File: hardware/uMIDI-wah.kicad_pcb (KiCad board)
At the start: 2 copper layers, 60 parts, among them IC1 Opamp_Dual_Generic, IC2 L78L09_SOT89, J1 Conn_01x10, Q1 BC547, Q2 BC547, Q3 BC547, SW1 MMP221, X1 AudioJack3_Switch, X3 AudioJack3_Switch

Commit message: Complete initial placement
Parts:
- C2, D1, D2, D5, D6, IC1, L1, L2, LDR1, LDR2, Q1, Q2, Q3, REL1, RV1, RV2, RV3, SW1, X1, X3: moved to B.Cu
- R10, R11: value 1M -> 100M
- X4: renamed from J1; moved to B.Cu
- moved LDR2 549.9 mm to (166.5, 122.0), turned to 90 degrees
- moved C8 526.2 mm to (182.5, 127.0), turned to 180 degrees
- moved R15 525.5 mm to (182.5, 123.5)
- moved D2 524.7 mm to (166.5, 123.5), turned to 180 degrees
- moved Q2 523.7 mm to (176.2, 123.5)
- moved R14 523.0 mm to (178.0, 127.0)
- moved C9 520.9 mm to (171.5, 117.5)
- moved D6 517.8 mm to (166.5, 120.0)
- moved R24 517.0 mm to (171.5, 120.0)
- moved X3 511.9 mm to (100.0, 135.0), turned to 90 degrees
- moved X4 498.8 mm to (194.0, 115.0)
- moved R11 479.0 mm to (112.5, 141.0)
- moved C7 463.8 mm to (171.5, 102.0)
- moved RV1 463.4 mm to (149.0, 122.0), turned to 90 degrees
- moved C6 457.8 mm to (138.0, 119.0)
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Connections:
- R5 pad 2: (no net) -> /bypass_n
- SW1 pad 3: Net-(L2-Pad1) -> Net-(L2-Pad2)
- SW1 pad 6: Net-(L2-Pad2) -> Net-(L2-Pad1)
- X4 pad 7: (no net) -> /bypass_n
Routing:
- net GND: vias 0 -> 3
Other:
- board outline added: 100 x 80 mm

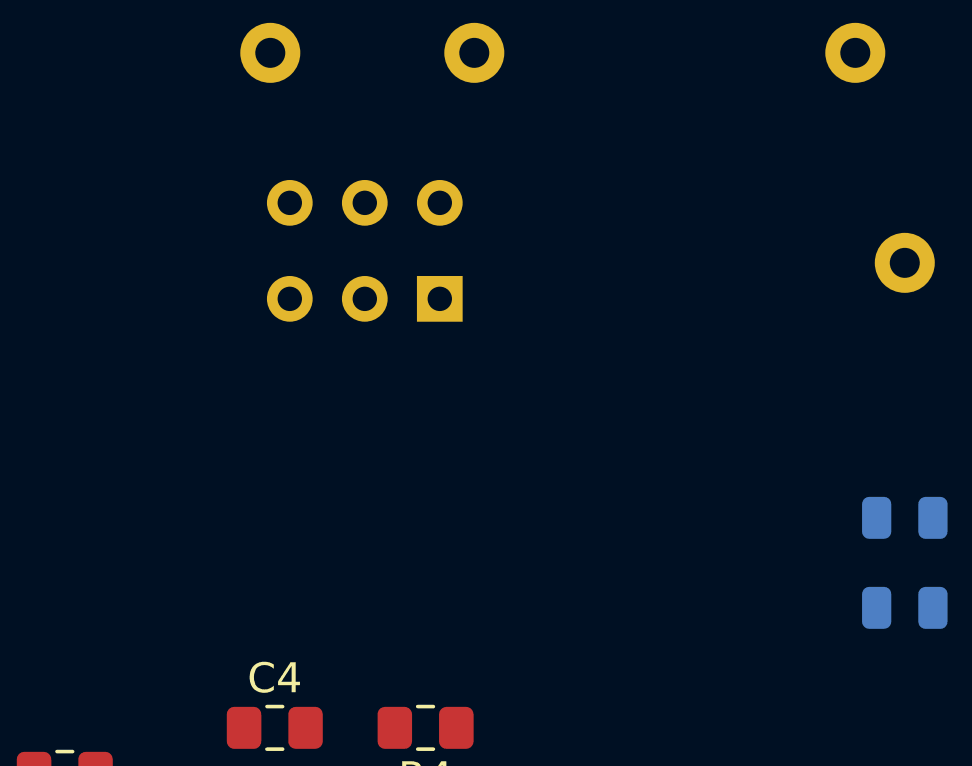
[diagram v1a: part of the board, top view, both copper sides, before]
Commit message: Use second relay to switch between inductors
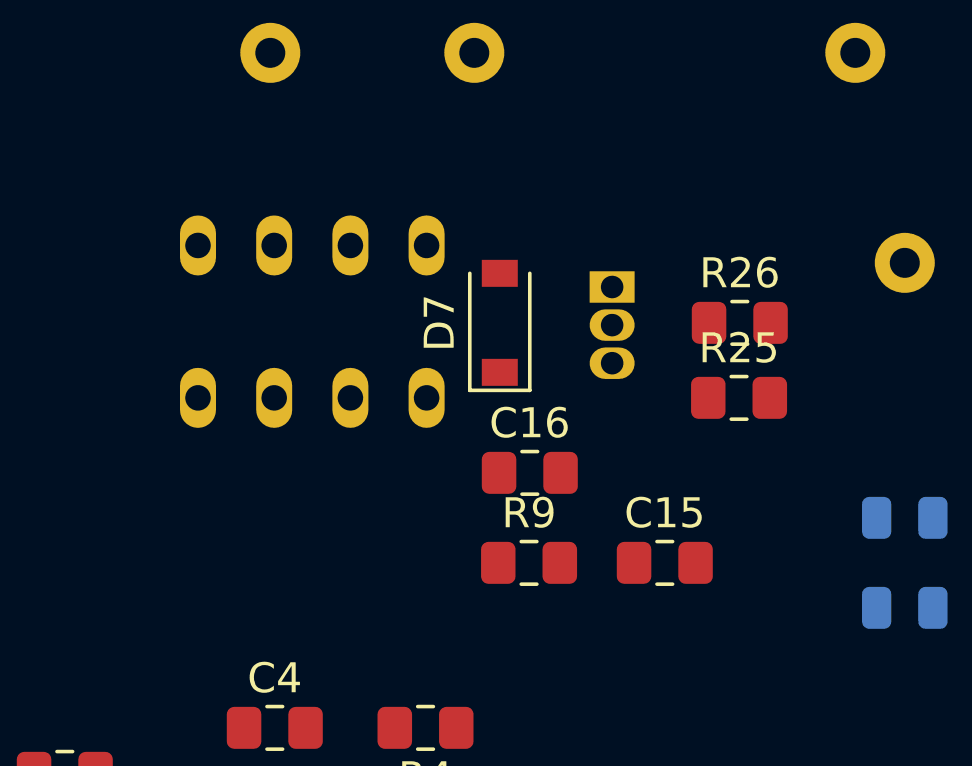
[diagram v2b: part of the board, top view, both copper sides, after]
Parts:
- removed SW1: MMP221, umidi-wah:MMP221
- added C15: 100n, Capacitor_SMD:C_0805_2012Metric_Pad1.15x1.40mm_HandSolder, F.Cu at (158.5, 98.0)
- added C16: 100n, Capacitor_SMD:C_0805_2012Metric_Pad1.15x1.40mm_HandSolder, F.Cu at (154.0, 95.0)
- added D7: 1N4148, Diode_SMD:D_SOD-123, F.Cu at (153.0, 90.0)
- added Q4: BC547, Package_TO_SOT_THT:TO-92_Inline, B.Cu at (156.7, 88.8)
- added R25: 1k, Resistor_SMD:R_0805_2012Metric_Pad1.15x1.40mm_HandSolder, F.Cu at (161.0, 92.5)
- added R26: 100M, Resistor_SMD:R_0805_2012Metric_Pad1.15x1.40mm_HandSolder, F.Cu at (161.0, 90.0)
- added R9: 180, Resistor_SMD:R_0805_2012Metric_Pad1.15x1.40mm_HandSolder, F.Cu at (154.0, 98.0)
- added REL2: Omron G6K-2P-5VCD, umidi-wah:Omron_G6K-2P, B.Cu at (146.7, 90.0)
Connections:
- X4 pad 6: GND -> /Fasel

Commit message: Place & route
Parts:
- moved C2 80.7 mm to (130.5, 136.2), turned to 270 degrees
- moved X4 71.7 mm to (128.0, 143.2), turned to 270 degrees
- moved C3 70.5 mm to (152.0, 142.2)
- moved C13 67.1 mm to (136.5, 138.7), turned to 0 degrees
- moved D4 66.9 mm to (145.5, 143.2), turned to 180 degrees
- moved IC2 65.3 mm to (141.5, 137.2), turned to 0 degrees
- moved C14 62.8 mm to (136.5, 135.7), turned to 0 degrees
- moved C12 36.8 mm to (125.4, 125.2), turned to 270 degrees
- moved C8 35.6 mm to (148.5, 137.6), turned to 90 degrees
- moved R22 35.4 mm to (128.0, 125.2), turned to 270 degrees
- moved R21 34.4 mm to (130.5, 125.2), turned to 90 degrees
- moved R15 33.6 mm to (152.0, 137.6), turned to 270 degrees
- moved C15 30.5 mm to (128.0, 98.5), turned to 270 degrees
- moved R13 30.2 mm to (152.8, 101.8), turned to 90 degrees
- moved R14 30.1 mm to (148.5, 133.2), turned to 270 degrees
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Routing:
- net /Vref: track 0.00 -> 84.4 mm, vias 0 -> 1
- net /PWM_Q: track 0.00 -> 69.4 mm
- net /q: track 0.00 -> 63.2 mm
- net /Fasel: track 0.00 -> 57.3 mm, vias 0 -> 1
- net /LED_Supply: track 0.00 -> 54.8 mm
- net /VDDa: track 0.00 -> 50.0 mm, vias 0 -> 2
- net /wah: track 0.00 -> 41.7 mm, vias 0 -> 1
- net /bypass_n: track 0.00 -> 40.5 mm
- net Net-(L1-Pad1): track 0.00 -> 32.7 mm
- net /Bypass/Loop_In: track 0.00 -> 32.6 mm
- net +9V: track 0.00 -> 26.0 mm
- net Net-(C6-Pad2): track 0.00 -> 23.4 mm
- net /PWM_Wah: track 0.00 -> 22.7 mm, vias 0 -> 1
- net Net-(C4-Pad1): track 0.00 -> 22.4 mm
- net Net-(D1-Pad1): track 0.00 -> 19.5 mm
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- added copper zone on B.Cu, net GND
- added copper zone on F.Cu, net GND
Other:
- board size 100 x 80 mm -> 63.5 x 80 mm

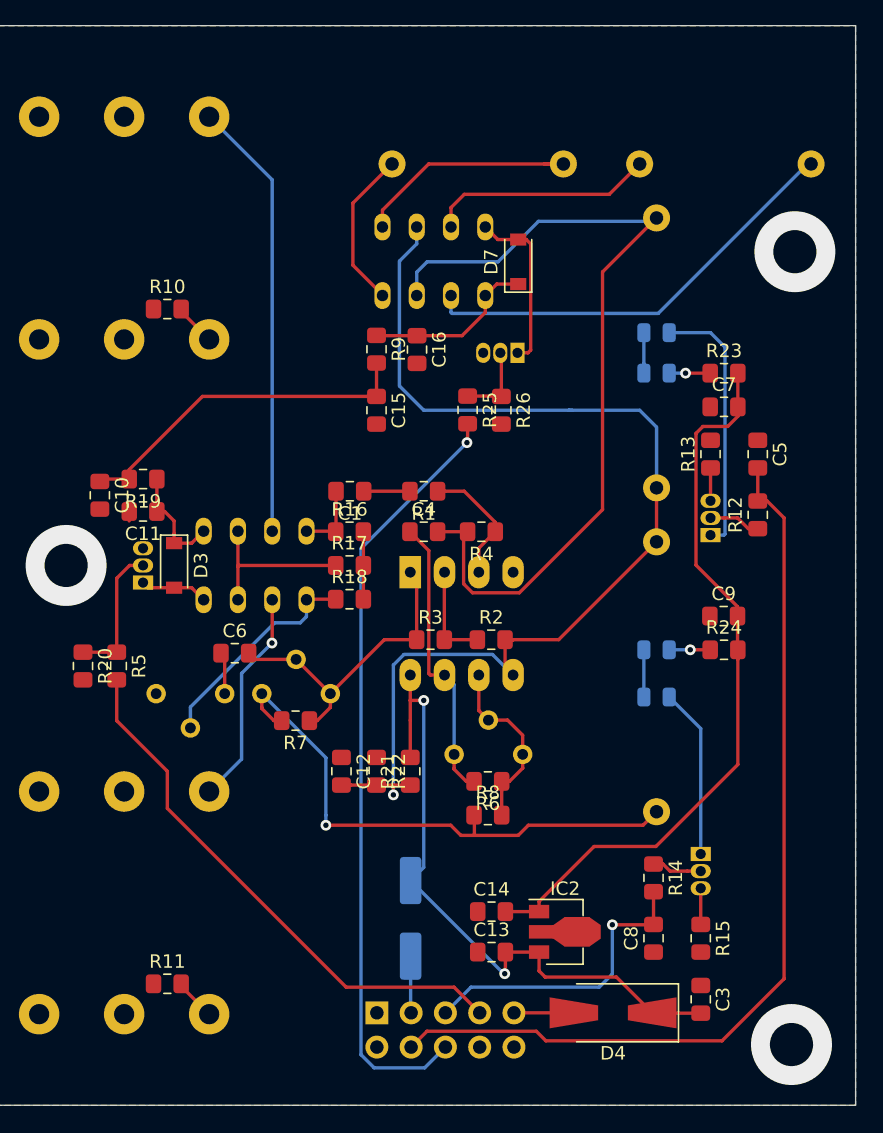
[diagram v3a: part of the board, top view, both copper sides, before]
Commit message: Optimize place & route, add label and OSHW logo
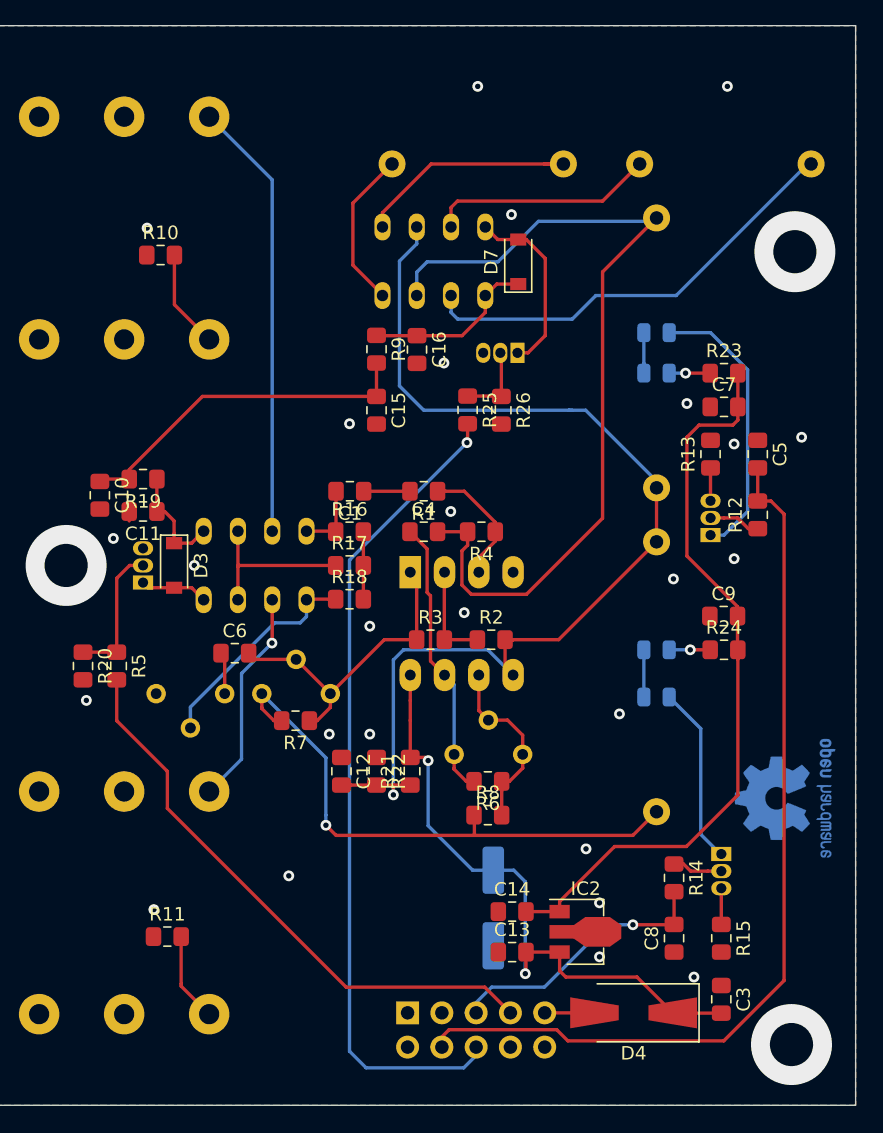
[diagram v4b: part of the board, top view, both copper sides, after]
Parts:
- added REF**: OSHW-Logo2_9.8x8mm_Copper, Symbol:OSHW-Logo2_9.8x8mm_Copper, B.Cu at (158.3, 127.3)
- moved C2 6.17 mm to (136.7, 135.4)
- moved R10 4.03 mm to (112.0, 87.0)
- moved R11 3.50 mm to (112.5, 137.5)
- moved X4 2.28 mm to (130.3, 143.2)
- moved C13 1.52 mm to (138.0, 138.7)
- moved C14 1.52 mm to (138.0, 135.7)
- moved C3 1.52 mm to (153.5, 142.2)
- moved C8 1.52 mm to (150.0, 137.6)
- moved D4 1.52 mm to (147.0, 143.2)
- moved IC2 1.52 mm to (143.0, 137.2)
- moved Q2 1.52 mm to (153.5, 131.4)
- moved R14 1.52 mm to (150.0, 133.2)
- moved R15 1.52 mm to (153.5, 137.6)
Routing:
- net GND: track 8.12 -> 3.85 mm, vias 3 -> 29
- net Net-(R10-Pad2): track 3.11 -> 7.32 mm
- net /Fasel: track 57.3 -> 61.0 mm
- net Net-(R11-Pad2): track 3.11 -> 6.61 mm
- net /VDDa: track 50.0 -> 47.5 mm
- net /bypass_n: track 40.5 -> 42.8 mm
- net /PWM_Wah: track 22.7 -> 20.6 mm
- net /Vref: track 84.4 -> 82.5 mm
- net Net-(D1-Pad1): track 19.5 -> 20.9 mm
- net /PWM_Q: track 69.4 -> 68.2 mm
- net /q: track 63.2 -> 64.1 mm
- net /Inductor/relais_n: track 12.8 -> 13.7 mm
- net /LED_Supply: track 54.8 -> 55.6 mm
- net Net-(D2-Pad1): track 12.6 -> 13.3 mm
- net Net-(C4-Pad1): track 22.4 -> 21.7 mm
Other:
- rule trace_min: 0.2 -> 0
- board text added: "uMIDI Wah v0.4"

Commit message: Fix relais supply
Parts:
- removed REF**: OSHW-Logo2_9.8x8mm_Copper, Symbol:OSHW-Logo2_9.8x8mm_Copper
- C5, C8: value 10uF -> 10u
- C7, C9: value 100nF -> 100n
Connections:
- C10 pad 1: +9V -> /+9V
- C14 pad 2: /LED_Supply -> /+9V
- C15 pad 1: +9V -> /+9V
- C7 pad 2: /LED_Supply -> /+9V
- C9 pad 2: /LED_Supply -> /+9V
- IC2 pad 1: /LED_Supply -> /+9V
- R19 pad 2: +9V -> /+9V
- R23 pad 2: /LED_Supply -> /+9V
- R24 pad 2: /LED_Supply -> /+9V
- R9 pad 2: +9V -> /+9V
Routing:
- net /+9V: track 0.00 -> 110.3 mm, vias 0 -> 2
- net /LED_Supply: track 55.6 -> 0.00 mm
- net +9V: track 26.0 -> 0.00 mm

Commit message: Add in-/output labels to audio jacks
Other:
- board text added: "Input"
- board text added: "Output"
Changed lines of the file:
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@@
   (general
     (thickness 1.6)
-    (drawings 7)
+    (drawings 9)
     (tracks 350)
     (zones 0)
@@
       (net 43 /Inductor/relais_n))
   )
+  (gr_text Output (at 124 135 90) (layer B.Mask)
+    (effects (font (size 1.5 1.5) (thickness 0.3)) (justify mirror))
+  )
+  (gr_text Input (at 124 84.5 90) (layer B.Mask)
+    (effects (font (size 1.5 1.5) (thickness 0.3)) (justify mirror))
+  )
   (gr_text "uMIDI Wah v0.4" (at 161.2 100.5 90) (layer B.Mask)
